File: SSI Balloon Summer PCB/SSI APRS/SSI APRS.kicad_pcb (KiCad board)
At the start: 4 copper layers, 80 x 45 mm, 25 parts, among them J1 Conn_01x08, J4 APRS antenna, U12 TPS63070RNMR, U5 DRA818V

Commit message: Various rewiring: SWD, microSD, APRS JST
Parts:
- removed R11, R12: 10k, Resistor_SMD:R_0603_1608Metric

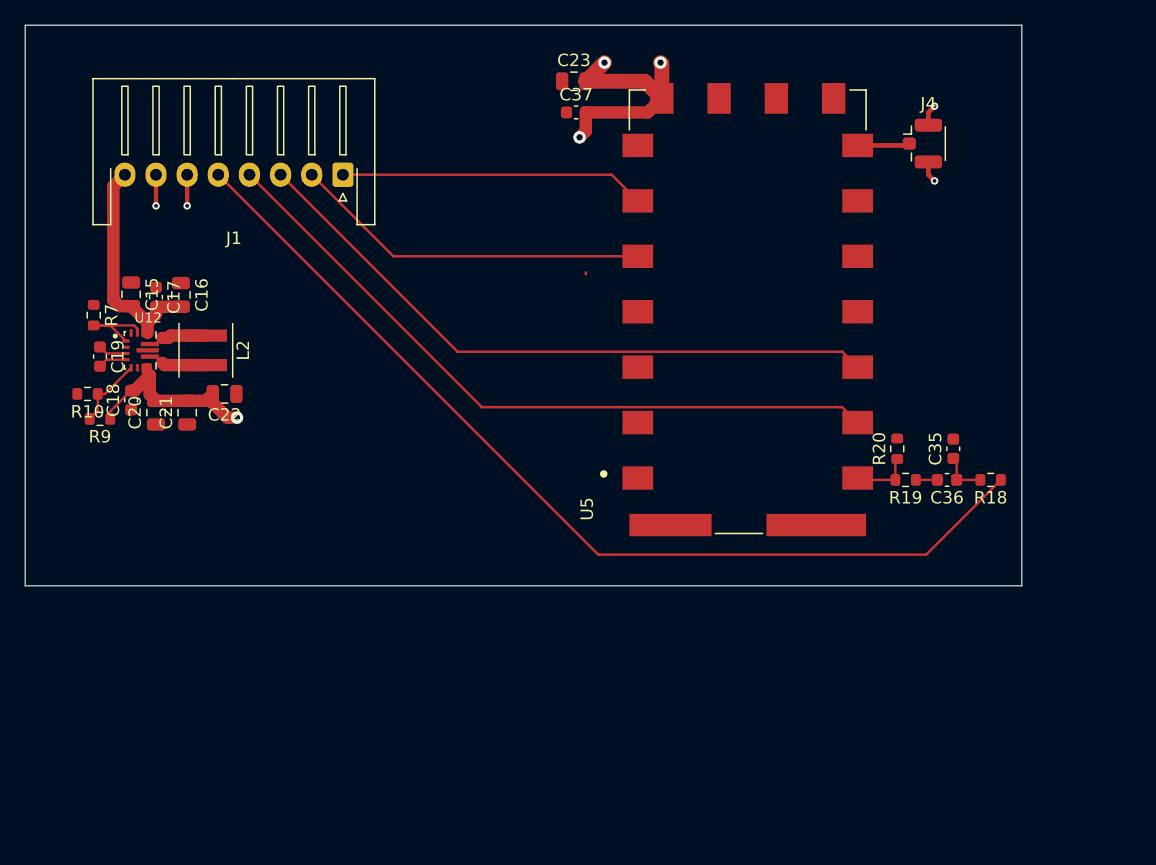
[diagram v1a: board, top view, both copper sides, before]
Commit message: Cleaned APRS Filter up and adding Testing points
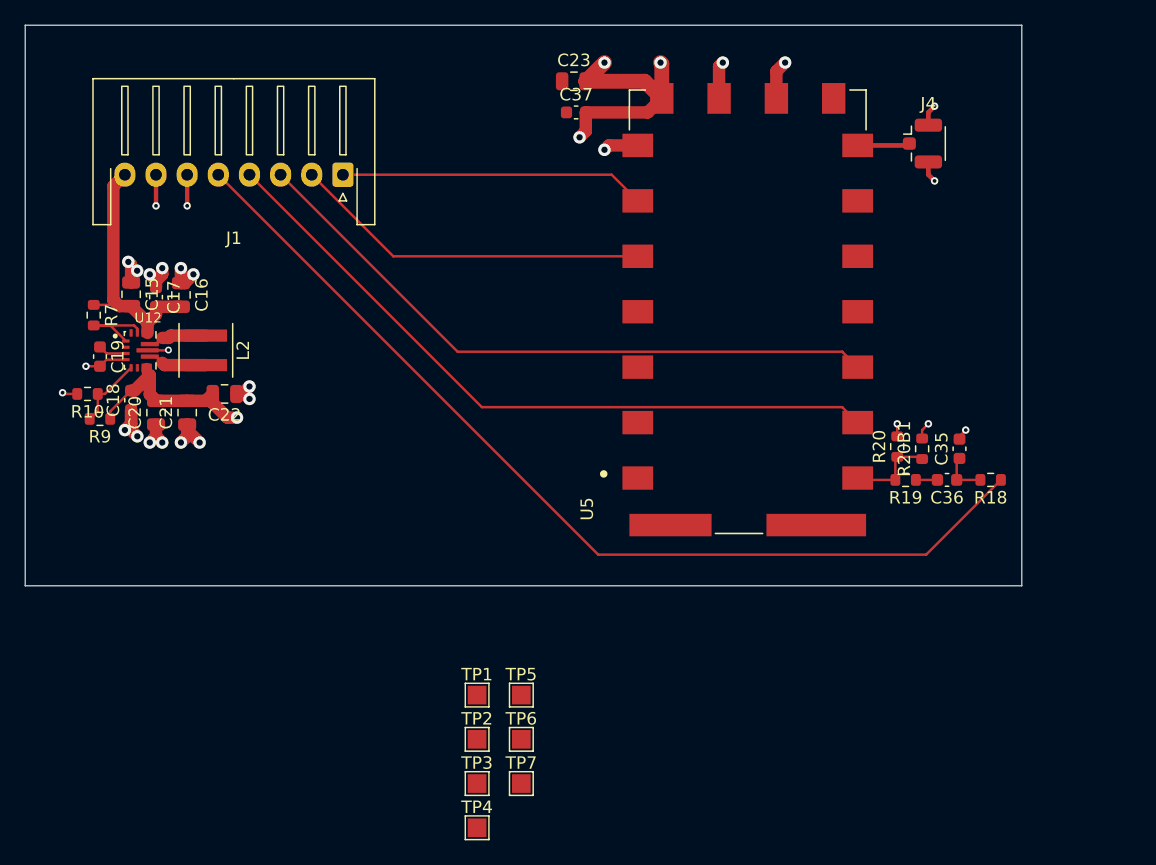
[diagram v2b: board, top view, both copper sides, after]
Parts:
- added R20B1: TBD, Resistor_SMD:R_0603_1608Metric, F.Cu at (172.0, 116.5)
- added TP1: TestPoint, TestPoint:TestPoint_Pad_1.5x1.5mm, F.Cu at (136.3, 136.3)
- added TP2: TestPoint, TestPoint:TestPoint_Pad_1.5x1.5mm, F.Cu at (136.3, 139.8)
- added TP3: TestPoint, TestPoint:TestPoint_Pad_1.5x1.5mm, F.Cu at (136.3, 143.4)
- added TP4: TestPoint, TestPoint:TestPoint_Pad_1.5x1.5mm, F.Cu at (136.3, 146.9)
- added TP5: TestPoint, TestPoint:TestPoint_Pad_1.5x1.5mm, F.Cu at (139.8, 136.3)
- added TP6: TestPoint, TestPoint:TestPoint_Pad_1.5x1.5mm, F.Cu at (139.8, 139.8)
- added TP7: TestPoint, TestPoint:TestPoint_Pad_1.5x1.5mm, F.Cu at (139.8, 143.4)
- R20: value 100 -> 470
- moved C35 0.50 mm to (175.0, 116.5)
- moved R20 0.17 mm to (170.0, 116.3)
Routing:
- net GND: track 10.8 -> 47.0 mm, vias 4 -> 27
- net Net-(U5-MIC_IN): track 4.82 -> 6.90 mm
- net +5V: track 18.5 -> 20.2 mm

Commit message: Finished test points
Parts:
- moved APRS_PTT 52.5 mm to (136.5, 91.0)
- moved APRS_AUDIO 49.3 mm to (136.5, 87.0)
- moved APRS_PD 45.4 mm to (136.5, 94.5)
- moved +5V_TEST1 30.8 mm to (110.5, 123.0)
- moved +4V1 27.7 mm to (115.5, 123.0)
- moved GND2 26.4 mm to (125.0, 123.0)
- moved GND1 25.8 mm to (120.5, 123.0)
- renumbered TP5 to +4V1, TP2 to +5V_TEST1, TP1 to APRS_AUDIO, TP6 to APRS_PD, TP7 to APRS_PTT, TP3 to GND1, TP4 to GND2
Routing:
- net +5V: track 20.2 -> 54.5 mm
- net /APRS_AUDIO: track 77.9 -> 102.1 mm
- net /APRS_PTT: track 29.4 -> 44.4 mm
- net GND: track 47.0 -> 51.0 mm, vias 27 -> 29
- net +4V1: track 36.4 -> 38.4 mm, vias 4 -> 5
- net /APRS_PD: track 24.5 -> 26.5 mm
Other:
- board text added: "+5V"
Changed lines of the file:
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@@
 	(footprint "TestPoint:TestPoint_Pad_1.5x1.5mm"
 		(layer "F.Cu")
-		(at 136.275 143.375)
+		(at 120.5 123)
 		(descr "SMD rectangular pad as test Point, square 1.5mm side length")
 		(tags "test point SMD pad rectangle square")
-		(property "Reference" "TP3"
-			(at 0 -1.648 0)
+		(property "Reference" "GND1"
+			(at 0 -2.998 0)
 			(layer "F.SilkS")
 			(effects
@@
 		)
 		(fp_text user "${REFERENCE}"
-			(at 0 -1.65 0)
+			(at 0 -3 0)
 			(layer "F.Fab")
 			(effects
@@
 	(footprint "TestPoint:TestPoint_Pad_1.5x1.5mm"
 		(layer "F.Cu")
-		(at 139.825 139.825)
+		(at 136.5 94.5)
 		(descr "SMD rectangular pad as test Point, square 1.5mm side length")
 		(tags "test point SMD pad rectangle square")
-		(property "Reference" "TP6"
+		(property "Reference" "APRS_PD"
 			(at 0 -1.648 0)
 			(layer "F.SilkS")
@@
 	(footprint "TestPoint:TestPoint_Pad_1.5x1.5mm"
 		(layer "F.Cu")
-		(at 136.275 146.925)
+		(at 125 123)
 		(descr "SMD rectangular pad as test Point, square 1.5mm side length")
 		(tags "test point SMD pad rectangle square")
-		(property "Reference" "TP4"
-			(at 0 -1.648 0)
+		(property "Reference" "GND2"
+			(at 0 -2.998 0)
 			(layer "F.SilkS")
 			(effects
@@
 		)
 		(fp_text user "${REFERENCE}"
-			(at 0 -1.65 0)
+			(at 0 -3 0)
 			(layer "F.Fab")
 			(effects
@@
 	(footprint "TestPoint:TestPoint_Pad_1.5x1.5mm"
 		(layer "F.Cu")
-		(at 136.275 139.825)
+		(at 110.5 123)
 		(descr "SMD rectangular pad as test Point, square 1.5mm side length")
 		(tags "test point SMD pad rectangle square")
-		(property "Reference" "TP2"
-			(at 0 -1.648 0)
+		(property "Reference" "+5V_TEST1"
+			(at 0 -3 0)
 			(layer "F.SilkS")
+			(hide yes)
 			(effects
 				(font
@@
 		)
 		(fp_text user "${REFERENCE}"
-			(at 0 -1.65 0)
+			(at 0 -3 0)
 			(layer "F.Fab")
 			(effects
@@
 	(footprint "TestPoint:TestPoint_Pad_1.5x1.5mm"
 		(layer "F.Cu")
-		(at 136.275 136.275)
+		(at 136.5 87)
 		(descr "SMD rectangular pad as test Point, square 1.5mm side length")
 		(tags "test point SMD pad rectangle square")
-		(property "Reference" "TP1"
+		(property "Reference" "APRS_AUDIO"
 			(at 0 -1.648 0)
 			(layer "F.SilkS")
@@
 		)
 		(property "Value" "TestPoint"
-			(at 0 1.75 0)
+			(at 0 1.5 0)
 			(layer "F.Fab")
 			(effects
@@
 	(footprint "TestPoint:TestPoint_Pad_1.5x1.5mm"
 		(layer "F.Cu")
-		(at 139.825 143.375)
+		(at 136.5 91)
 		(descr "SMD rectangular pad as test Point, square 1.5mm side length")
 		(tags "test point SMD pad rectangle square")
-		(property "Reference" "TP7"
-			(at 0 -1.648 0)
+		(property "Reference" "APRS_PTT"
+			(at 0 -1.898 0)
 			(layer "F.SilkS")
 			(effects
@@
 		)
 		(fp_text user "${REFERENCE}"
-			(at 0 -1.65 0)
+			(at 0 -1.9 0)
 			(layer "F.Fab")
 			(effects
@@
 	(footprint "TestPoint:TestPoint_Pad_1.5x1.5mm"
 		(layer "F.Cu")
-		(at 139.825 136.275)
+		(at 115.5 123)
 		(descr "SMD rectangular pad as test Point, square 1.5mm side length")
 		(tags "test point SMD pad rectangle square")
-		(property "Reference" "TP5"
-			(at 0 -1.648 0)
+		(property "Reference" "+4V1"
+			(at 0.5 -2.998 0)
 			(layer "F.SilkS")
 			(effects
@@
 		)
 		(fp_text user "${REFERENCE}"
-			(at 0 -1.65 0)
+			(at 0.5 -3 0)
 			(layer "F.Fab")
 			(effects
@@
 		(layer "Edge.Cuts")
 	)
+	(gr_text "+5V\n"
+		(at 110.5 120 0)
+		(layer "F.SilkS")
+		(effects
+			(font
+				(size 1 1)
+				(thickness 0.15)
+			)
+		)
+	)
 	(segment
 		(start 108.075 109.35)
@@
 	)
 	(segment
+		(start 125 123)
+		(end 125 121)
+		(width 1)
+		(layer "F.Cu")
+		(net "GND")
+	)
+	(segment
 		(start 113 114.55)
 		(end 113 115.5)
@@
 	)
 	(segment
+		(start 120.5 123)
+		(end 120.5 121)
+		(width 1)
+		(layer "F.Cu")
+		(net "GND")
+	)
+	(segment
 		(start 111.475 108.6)
 		(end 111.5 108.575)
@@
 	)
 	(via
+		(at 125 121)
+		(size 1)
+		(drill 0.5)
+		(layers "F.Cu" "B.Cu")
+		(net "GND")
+	)
+	(via
+		(at 120.5 121)
+		(size 1)
+		(drill 0.5)
+		(layers "F.Cu" "B.Cu")
+		(net "GND")
+	)
+	(via
 		(at 113.5 102.5)
 		(size 1)
@@
 	)
 	(segment
+		(start 101 105.575)
+		(end 101 121)
+		(width 1)
+		(layer "F.Cu")
+		(net "+5V")
+	)
+	(segment
+		(start 107.075 99.5)
+		(end 101 105.575)
+		(width 1)
+		(layer "F.Cu")
+		(net "+5V")
+	)
+	(segment
 		(start 108 94.5)
 		(end 107.075 95.425)
@@
 	)
 	(segment
+		(start 101 121)
+		(end 103 123)
+		(width 1)
+		(layer "F.Cu")
+		(net "+5V")
+	)
+	(segment
 		(start 108.4 104.95)
 		(end 108.5 105.05)
@@
 	)
 	(segment
+		(start 107.075 95.425)
+		(end 107.075 99.5)
+		(width 1)
+		(layer "F.Cu")
+		(net "+5V")
+	)
+	(segment
 		(start 110.5 105.7)
 		(end 109.825 106.375)
@@
 	)
 	(segment
-		(start 107.075 95.425)
+		(start 103 123)
+		(end 110.5 123)
+		(width 1)
+		(layer "F.Cu")
+		(net "+5V")
+	)
+	(segment
+		(start 107.075 99.5)
 		(end 107.075 104.575)
 		(width 1)
@@
 	)
 	(segment
+		(start 115.5 94.5)
+		(end 123 87)
+		(width 0.2)
+		(layer "F.Cu")
+		(net "/APRS_AUDIO")
+	)
+	(segment
 		(start 146 125)
 		(end 172.325 125)
@@
 	)
 	(segment
+		(start 123 87)
+		(end 136.5 87)
+		(width 0.2)
+		(layer "F.Cu")
+		(net "/APRS_AUDIO")
+	)
+	(segment
 		(start 174.775 119)
 		(end 174.775 117.55)
@@
 	)
 	(segment
+		(start 125.5 94.5)
+		(end 127 96)
+		(width 0.2)
+		(layer "F.Cu")
+		(net "/APRS_PD")
+	)
+	(segment
+		(start 136.5 96)
+		(end 148.575 96)
+		(width 0.2)
+		(layer "F.Cu")
+		(net "/APRS_PD")
+	)
+	(segment
+		(start 127 96)
+		(end 136.5 96)
+		(width 0.2)
+		(layer "F.Cu")
+		(net "/APRS_PD")
+	)
+	(segment
+		(start 148.575 96)
+		(end 149.175 96.6)
+		(width 0.2)
+		(layer "F.Cu")
+		(net "/APRS_PD")
+	)
+	(segment
+		(start 136.5 96)
+		(end 136.5 94)
+		(width 0.2)
+		(layer "F.Cu")
+		(net "/APRS_PD")
+	)
+	(segment
 		(start 111 107.6)
 		(end 111.5 107.6)
@@
 	)
 	(segment
-		(start 148.8 100.675)
-		(end 149.175 101.05)
+		(start 123 94.5)
+		(end 126.5 91)
 		(width 0.2)
 		(layer "F.Cu")
@@
 	)
 	(segment
-		(start 129.55 101.05)
-		(end 149.175 101.05)
+		(start 126.5 91)
+		(end 136.5 91)
 		(width 0.2)
 		(layer "F.Cu")
@@
 	)
 	(segment
-		(start 147.075 94.5)
-		(end 149.175 96.6)
+		(start 148.8 100.675)
+		(end 149.175 101.05)
 		(width 0.2)
 		(layer "F.Cu")
-		(net "/APRS_PD")
+		(net "/APRS_PTT")
 	)
 	(segment
-		(start 125.5 94.5)
-		(end 147.075 94.5)
+		(start 129.55 101.05)
+		(end 149.175 101.05)
 		(width 0.2)
 		(layer "F.Cu")
-		(net "/APRS_PD")
+		(net "/APRS_PTT")
 	)
 	(segment
@@
 	)
 	(segment
+		(start 115.5 123)
+		(end 115.5 121)
+		(width 1)
+		(layer "F.Cu")
+		(net "+4V1")
+	)
+	(segment
 		(start 110 112.15)
 		(end 110.225 112.375)
@@
 	)
 	(via
+		(at 115.5 121)
+		(size 1)
+		(drill 0.5)
+		(layers "F.Cu" "B.Cu")
+		(net "+4V1")
+	)
+	(via
 		(at 151 85.5)
 		(size 1)
@@
 		(polygon
 			(pts
-				(xy 114 114.483218) (xy 153 114.483218) (xy 153 83.983218) (xy 113.5 83.983218)
+				(xy 114.205193 127) (xy 153 127) (xy 153 83.983218) (xy 113.5 83.983218)
 			)
 		)

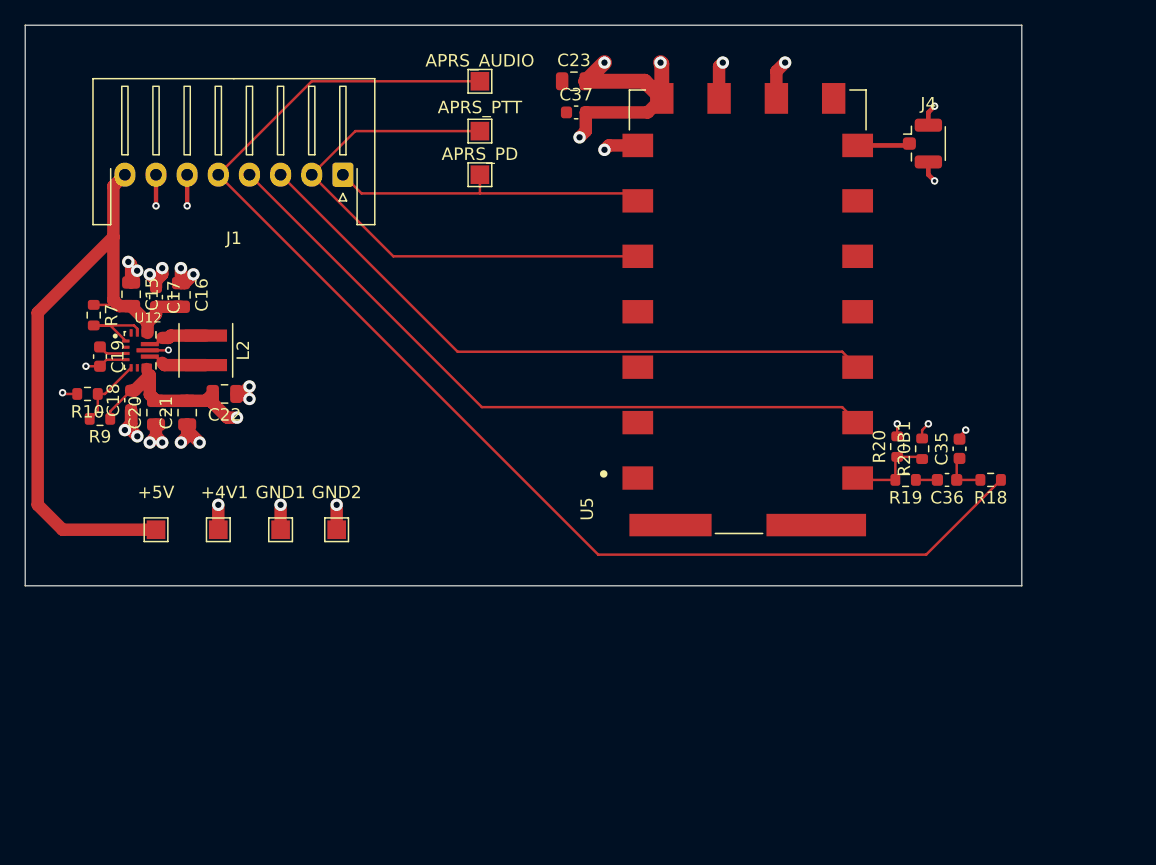
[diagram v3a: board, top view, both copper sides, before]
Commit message: Added Headers for testing, finalizing PCB
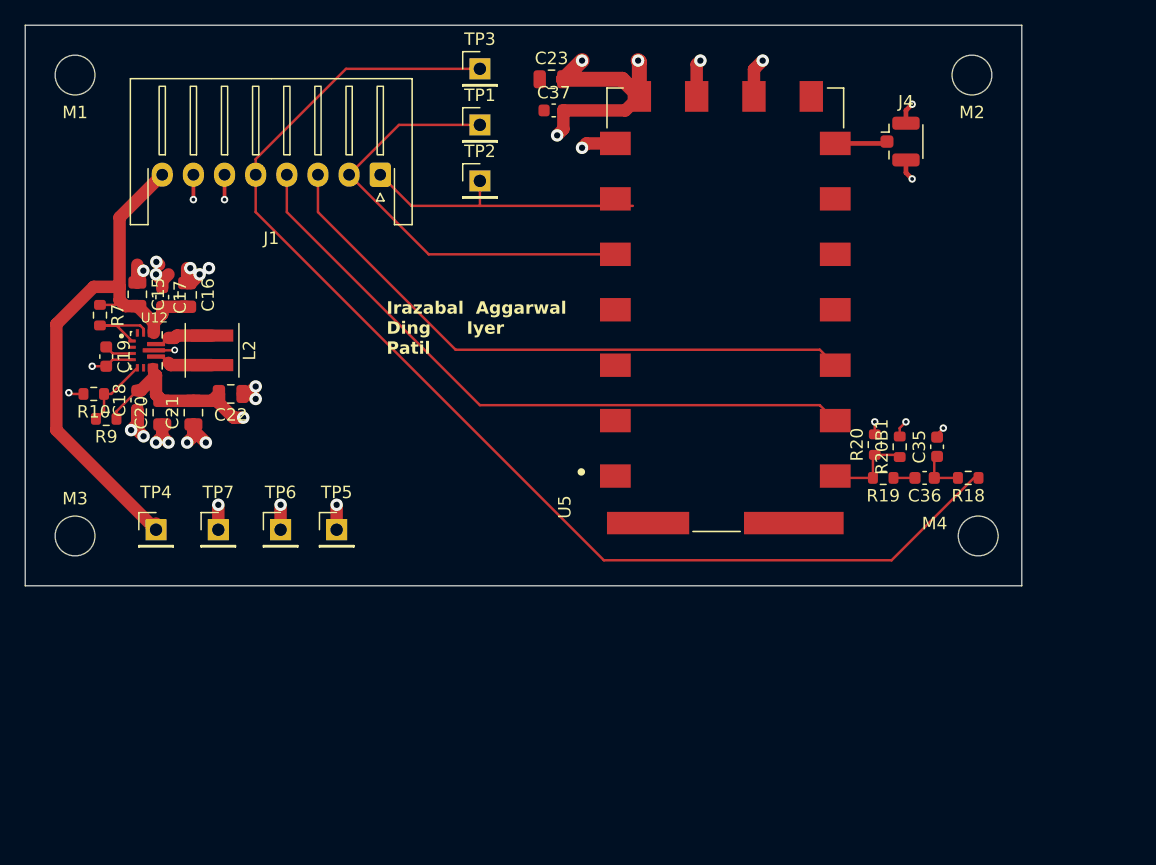
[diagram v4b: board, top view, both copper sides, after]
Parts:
- removed +4V1, +5V_TEST1, APRS_AUDIO, APRS_PD, APRS_PTT, GND1, GND2: TestPoint, TestPoint:TestPoint_Pad_1.5x1.5mm
- added M1: MountingHole_3.2mm_M3, MountingHole:MountingHole_3.2mm_M3, F.Cu at (104.0, 86.5)
- added M2: MountingHole_3.2mm_M3, MountingHole:MountingHole_3.2mm_M3, F.Cu at (176.0, 86.5)
- added M3: MountingHole_3.2mm_M3, MountingHole:MountingHole_3.2mm_M3, F.Cu at (104.0, 123.5)
- added M4: MountingHole_3.2mm_M3, MountingHole:MountingHole_3.2mm_M3, F.Cu at (176.5, 123.5)
- added TP1: Conn_01x01, Connector_PinHeader_2.54mm:PinHeader_1x01_P2.54mm_Vertical, F.Cu at (136.5, 90.5)
- added TP2: Conn_01x01, Connector_PinHeader_2.54mm:PinHeader_1x01_P2.54mm_Vertical, F.Cu at (136.5, 95.0)
- added TP3: Conn_01x01, Connector_PinHeader_2.54mm:PinHeader_1x01_P2.54mm_Vertical, F.Cu at (136.5, 86.0)
- added TP4: Conn_01x01, Connector_PinHeader_2.54mm:PinHeader_1x01_P2.54mm_Vertical, F.Cu at (110.5, 123.0)
- added TP5: Conn_01x01, Connector_PinHeader_2.54mm:PinHeader_1x01_P2.54mm_Vertical, F.Cu at (125.0, 123.0)
- added TP6: Conn_01x01, Connector_PinHeader_2.54mm:PinHeader_1x01_P2.54mm_Vertical, F.Cu at (120.5, 123.0)
- added TP7: Conn_01x01, Connector_PinHeader_2.54mm:PinHeader_1x01_P2.54mm_Vertical, F.Cu at (115.5, 123.0)
- moved J1 3.00 mm to (128.5, 94.5)
- moved C23 1.81 mm to (142.2, 86.8)
- moved C35 1.81 mm to (173.2, 116.3)
- moved C36 1.81 mm to (172.2, 118.8)
- moved J4 1.81 mm to (170.7, 91.8)
- moved R18 1.81 mm to (175.7, 118.8)
- moved R19 1.81 mm to (168.9, 118.8)
- moved R20 1.81 mm to (168.2, 116.2)
- moved R20B1 1.81 mm to (170.2, 116.3)
- moved U5 1.81 mm to (156.2, 105.3)
- moved C37 1.81 mm to (142.4, 89.3)
- moved C15 0.50 mm to (109.0, 104.1)
- moved C16 0.50 mm to (113.0, 104.2)
- moved C17 0.50 mm to (111.0, 104.3)
- moved C18 0.50 mm to (109.0, 112.6)
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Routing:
- net +5V: track 54.5 -> 47.9 mm
- net /APRS_PTT: track 44.4 -> 37.7 mm
- net /APRS_AUDIO: track 102.1 -> 97.6 mm
- net /APRS_TX: track 57.1 -> 54.0 mm
- net /APRS_RX: track 52.7 -> 49.6 mm
- net /APRS_PD: track 26.5 -> 23.9 mm
- net GND: track 51.0 -> 50.0 mm
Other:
- board text added: "Irazabal Aggarwal Ding Iyer Patil"
- board text removed: "+5V"
